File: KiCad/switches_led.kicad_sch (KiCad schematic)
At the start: 70 parts, among them Q2 2N3904, Q3 2N3904, Q4 2N3904, Q5 2N3904, Q6 2N3904, Q7 2N3904, Q8 2N3904, Q9 2N3904, SW9 SW_Rotary_1x9_MP, U2 CD4017BE

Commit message: adding missing SMD footprints
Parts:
- removed Q2, Q3, Q4, Q5, Q6, Q7, Q8, Q9: 2N3904, Package_TO_SOT_THT:TO-92_Inline, symbol Transistor_BJT:2N3904
- removed RV2, RV3, RV4, RV5, RV6, RV7, RV8, RV9: B100k, symbol Device:R_Potentiometer_US
- added Q1, Q2, Q3, Q4, Q5, Q6, Q7, Q8: MMBT3904, Package_TO_SOT_SMD:SOT-23, symbol Transistor_BJT:MMBT3904
- added RV2, RV3, RV4, RV5, RV6, RV7, RV8, RV9: 100k, Eurorack:RD901F, symbol Eurorack:RD901F
- D10, D11, D21, D22, D23, D24, D25, D26, D27, D28, D29, D4, D5, D6, D7, D8, D9: footprint Diode_THT:D_DO-35_SOD27_P7.62mm_Horizontal -> Diode_SMD:D_SOD-323_HandSoldering
- D12, D13, D14, D15, D16, D17, D18, D19: footprint LED_THT:LED_D3.0mm_IRBlack -> LED_THT:LED_D3.0mm_Clear
- R14, R15, R16, R17, R18, R19, R20, R21, R22, R23, R24, R25, R26, R27, R28, R29, R31: footprint (none) -> Resistor_SMD:R_0805_2012Metric_Pad1.20x1.40mm_HandSolder
- TP7: footprint (none) -> TestPoint:TestPoint_Pad_D1.5mm
- U2: footprint N16 -> Eurorack:CD4017BE THT
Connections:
- net Count0: now also RV2.3
- net Count1: now also RV3.3
- net Count2: now also RV4.3
- net Count3: now also RV5.3
- net Count4: now also RV6.3
- net Count5: now also RV7.3
- net Count6: now also RV8.3
- net Count7: now also RV9.3
- net GND: now also D27.2 (A), Q1.2 (E), Q2.2 (E), Q3.2 (E), Q4.2 (E), Q5.2 (E), Q6.2 (E), Q7.2 (E), Q8.2 (E), RV2.1, RV3.1, RV3.2, RV4.1, RV4.2, RV5.1, RV5.2, RV6.1, RV6.2, RV7.1, RV7.2, RV8.1, RV8.2, RV9.1, RV9.2
- net at D16.1 (K): now also Q6.3 (C)
- net at R28.1: now also Q1.1 (B)
- net at D19.1 (K): now also Q1.3 (C)
- net at D21.2 (A): now also RV2.2
- net at R14.1: now also Q2.1 (B)
- net at D12.1 (K): now also Q2.3 (C)
- net at D13.1 (K): now also Q3.3 (C)
- net at R24.1: now also Q7.1 (B)
- net at D17.1 (K): now also Q7.3 (C)
- net at R26.1: now also Q8.1 (B)
- net at D18.1 (K): now also Q8.3 (C)
- net at R16.1: now also Q3.1 (B)
- net at R20.1: now also Q5.1 (B)
- net at D15.1 (K): now also Q5.3 (C)
- net at R18.1: now also Q4.1 (B)
- net at R22.1: now also Q6.1 (B)
- net at D14.1 (K): now also Q4.3 (C)
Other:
- moved on the sheet: D21, D22, D23, D24, D25, D26, D27, D28, TP7

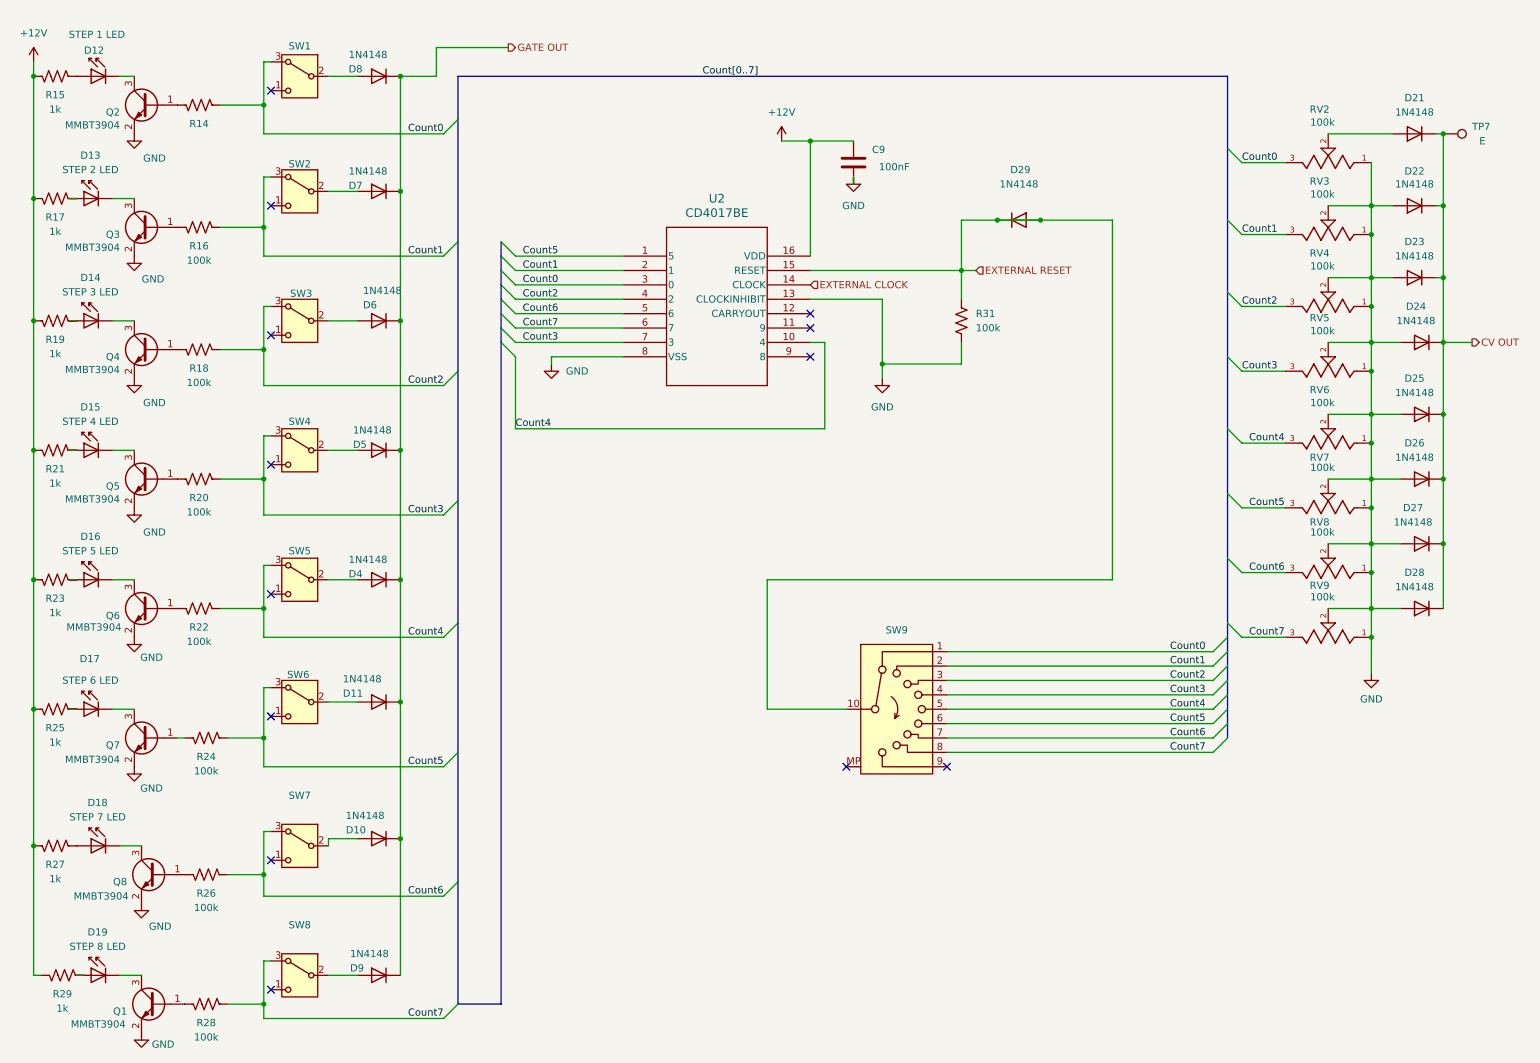
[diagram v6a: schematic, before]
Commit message: adding Test Point D
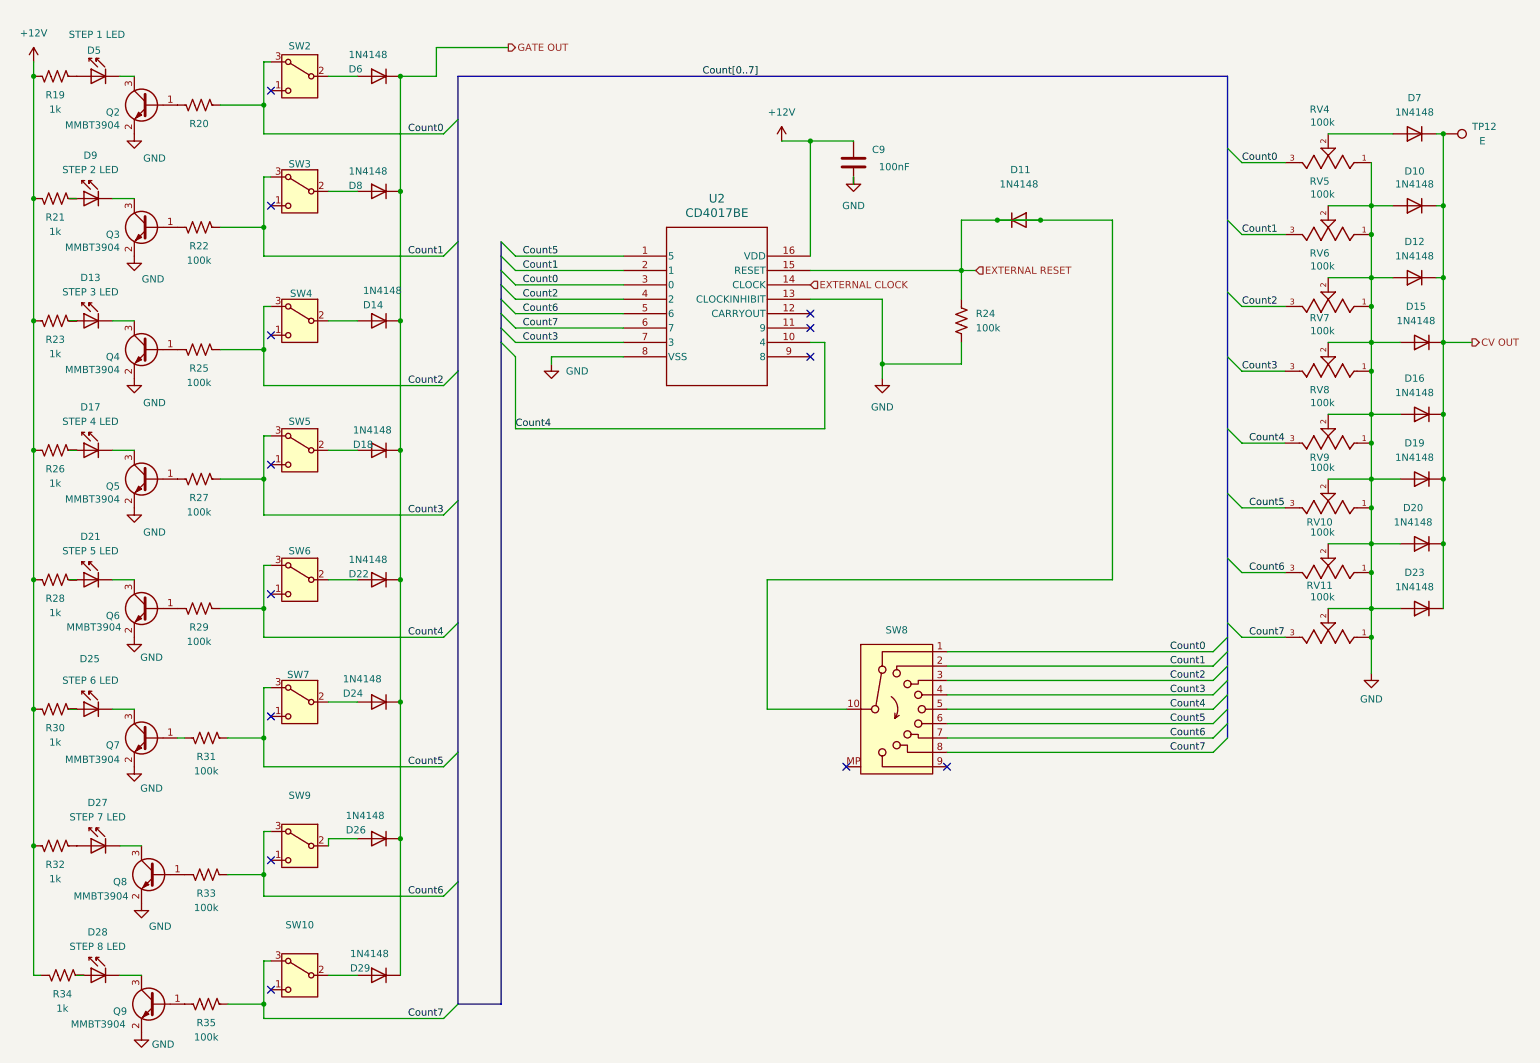
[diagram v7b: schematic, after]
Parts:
- renumbered D22 to D10, D29 to D11, D23 to D12, D14 to D13, D6 to D14, D24 to D15, D25 to D16, D15 to D17, D5 to D18, D26 to D19, D27 to D20, D16 to D21, D4 to D22, D28 to D23, D11 to D24, D17 to D25, D10 to D26, D18 to D27, D19 to D28, D9 to D29, D12 to D5, D8 to D6, D21 to D7, D7 to D8, D13 to D9, Q1 to Q9, R15 to R19, R14 to R20, R17 to R21, R16 to R22, R19 to R23, R31 to R24, R18 to R25, R21 to R26, R20 to R27, R23 to R28, R22 to R29, R25 to R30, R24 to R31, R27 to R32, R26 to R33, R29 to R34, R28 to R35, RV8 to RV10, RV9 to RV11, RV2 to RV4, RV3 to RV5, RV4 to RV6, RV5 to RV7, RV6 to RV8, RV7 to RV9, SW8 to SW10, SW1 to SW2, SW2 to SW3, SW3 to SW4, SW4 to SW5, SW5 to SW6, SW6 to SW7, SW9 to SW8, SW7 to SW9, TP7 to TP12

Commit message: adding footprints
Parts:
- SW10, SW2, SW3, SW4, SW5, SW6, SW7, SW9: footprint Button_Switch_SMD:Nidec_Copal_CAS-120A -> Eurorack:2MS1T1B1M2QES
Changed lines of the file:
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@@
 			)
 		)
-		(property "Footprint" "Button_Switch_SMD:Nidec_Copal_CAS-120A"
+		(property "Footprint" "Eurorack:2MS1T1B1M2QES"
 			(at 66.04 170.18 0)
 			(effects
@@
 			)
 		)
-		(property "Footprint" "Button_Switch_SMD:Nidec_Copal_CAS-120A"
+		(property "Footprint" "Eurorack:2MS1T1B1M2QES"
 			(at 66.04 100.33 0)
 			(effects
@@
 			)
 		)
-		(property "Footprint" "Button_Switch_SMD:Nidec_Copal_CAS-120A"
+		(property "Footprint" "Eurorack:2MS1T1B1M2QES"
 			(at 66.04 193.04 0)
 			(effects
@@
 			)
 		)
-		(property "Footprint" "Button_Switch_SMD:Nidec_Copal_CAS-120A"
+		(property "Footprint" "Eurorack:2MS1T1B1M2QES"
 			(at 66.04 144.78 0)
 			(effects
@@
 			)
 		)
-		(property "Footprint" "Button_Switch_SMD:Nidec_Copal_CAS-120A"
+		(property "Footprint" "Eurorack:2MS1T1B1M2QES"
 			(at 66.04 54.61 0)
 			(effects
@@
 			)
 		)
-		(property "Footprint" "Button_Switch_SMD:Nidec_Copal_CAS-120A"
+		(property "Footprint" "Eurorack:2MS1T1B1M2QES"
 			(at 66.04 34.29 0)
 			(effects
@@
 			)
 		)
-		(property "Footprint" "Button_Switch_SMD:Nidec_Copal_CAS-120A"
+		(property "Footprint" "Eurorack:2MS1T1B1M2QES"
 			(at 66.04 123.19 0)
 			(effects
@@
 			)
 		)
-		(property "Footprint" "Button_Switch_SMD:Nidec_Copal_CAS-120A"
+		(property "Footprint" "Eurorack:2MS1T1B1M2QES"
 			(at 66.04 77.47 0)
 			(effects
